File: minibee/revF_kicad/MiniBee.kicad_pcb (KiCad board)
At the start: 2 copper layers, 26.5 x 34 mm, 39 parts, among them IC1 MEGA8-AI, U1 ADXL345

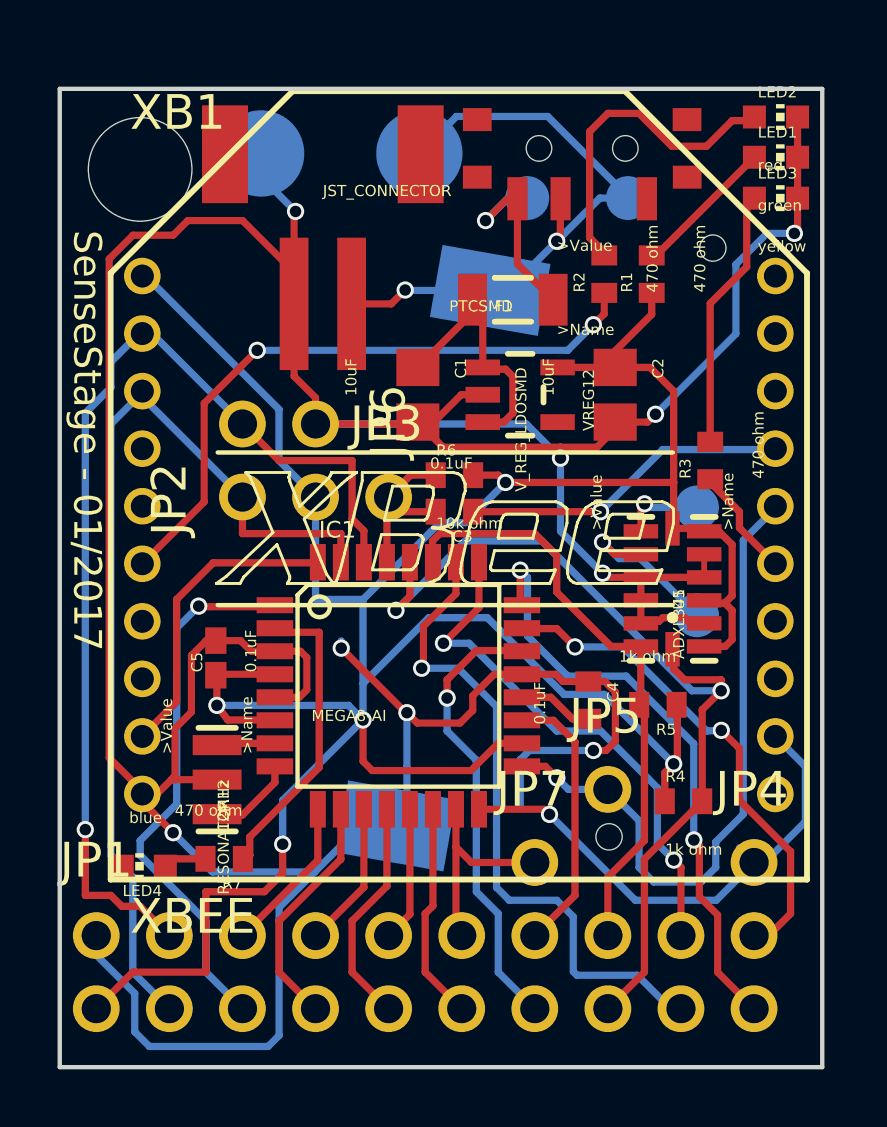
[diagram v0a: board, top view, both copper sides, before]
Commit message: updates to board: exchanged D2 and D7, other switch
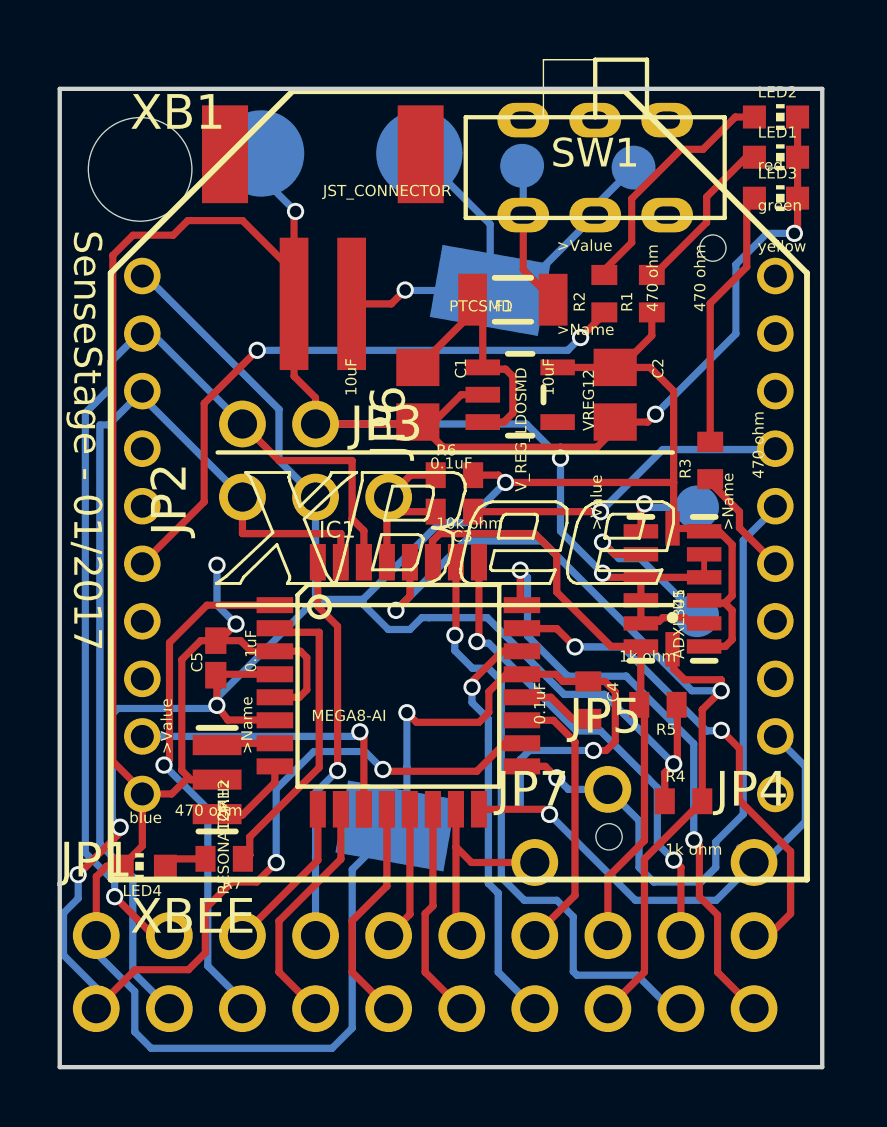
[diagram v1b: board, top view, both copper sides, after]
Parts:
- removed SWITCH12: MYSHIT_PCM_SWITCH, MYSHIT_PCM_SWITCH_RA
- added SW1: Switch_SPDT_x2, alps:alps_switch, F.Cu at (153.9, 90.7)
- moved JP11 1.14 mm to (151.3, 90.7)
- moved JP10 1.08 mm to (155.2, 90.7)
- moved R1 0.68 mm to (155.8, 95.1)
- moved R2 0.68 mm to (154.2, 95.1)
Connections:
- IC1 pad 32: /SLEEP -> /D2
- JP1 pad 8: /D7 -> /D2
- XB1 pad 9: /SLEEP -> /D7
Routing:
- net /D2: track 0.00 -> 13.6 mm, vias 0 -> 1
- net /SLEEP: track 10.7 -> 0.00 mm
- net VCC: track 105.7 -> 113.4 mm, vias 5 -> 7
- net /D7: track 5.09 -> 10.4 mm, vias 0 -> 1
- net /N$4: track 21.7 -> 18.3 mm, vias 2 -> 1
- net GND: track 153.4 -> 156.4 mm
- net /N$6: track 11.2 -> 8.48 mm
- net /N$8: track 7.22 -> 5.52 mm, vias 1 -> 0
- net /A3: track 22.9 -> 21.2 mm
- net /A2: track 18.3 -> 16.6 mm
- net /A7: track 15.7 -> 14.5 mm
- net /N$3: track 4.99 -> 5.79 mm
- net /D3: track 19.0 -> 18.2 mm
- net /TX: track 33.2 -> 33.9 mm
- net /PWM0: track 22.4 -> 21.7 mm

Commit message: updated gerbers for revision F
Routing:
- net GND: track 156.4 -> 157.0 mm, vias 9 -> 10
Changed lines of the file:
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@@
     (thickness 1.6)
     (drawings 138)
-    (tracks 528)
+    (tracks 532)
     (zones 0)
     (modules 39)
@@
   )
   (gr_line (start 149.953 98.6356) (end 150.10925 98.596537) (layer Eco1.User) (width 0.15))
+  (via (at 157.7213 97.5487) (size 0.6) (drill 0.4) (layers Top Bottom) (net 1))
+  (segment (start 157.6705 97.0153) (end 157.6705 97.4979) (width 0.25) (layer Top) (net 1))
+  (segment (start 157.6705 97.4979) (end 157.7213 97.5487) (width 0.25) (layer Top) (net 1))
   (segment (start 146.928355 113.620882) (end 146.928355 113.180345) (width 0.25) (layer Bottom) (net 1))
   (segment (start 151.3137 108.3496) (end 150.7685 108.3496) (width 0.25) (layer Top) (net 1))
@@
   (segment (start 158.75 94.107) (end 159.8295 93.0275) (width 0.25) (layer Bottom) (net 1))
   (segment (start 158.75 96.52) (end 158.75 94.107) (width 0.25) (layer Bottom) (net 1))
-  (segment (start 155.956 99.314) (end 158.75 96.52) (width 0.25) (layer Bottom) (net 1))
+  (segment (start 155.956 99.314) (end 157.7213 97.5487) (width 0.25) (layer Bottom) (net 1))
+  (segment (start 157.7213 97.5487) (end 158.75 96.52) (width 0.25) (layer Bottom) (net 1))
   (via (at 155.956 99.314) (size 0.6) (drill 0.4) (layers Top Bottom) (net 1))
   (segment (start 155.6844 99.5856) (end 155.956 99.314) (width 0.25) (layer Top) (net 1))
@@
   (segment (start 158.8731 103.2616) (end 158.8731 102.6996) (width 0.254) (layer Top) (net 33))
   (segment (start 160.1211 104.5096) (end 158.8731 103.2616) (width 0.254) (layer Top) (net 33))
-  (segment (start 157.8571 100.1596) (end 157.8571 95.4606) (width 0.254) (layer Top) (net 34))
-  (segment (start 157.8571 95.4606) (end 159.1271 94.1906) (width 0.254) (layer Top) (net 34))
-  (segment (start 159.1271 94.1906) (end 159.1271 92.0316) (width 0.254) (layer Top) (net 34))
+  (segment (start 157.8571 100.1596) (end 157.8571 99.8167) (width 0.254) (layer Top) (net 34))
+  (segment (start 157.8571 99.8167) (end 159.1271 98.5467) (width 0.254) (layer Top) (net 34))
+  (segment (start 159.1271 98.5467) (end 159.1271 92.0316) (width 0.254) (layer Top) (net 34))
   (segment (start 159.1271 92.0316) (end 159.3811 91.7776) (width 0.254) (layer Top) (net 34))
   (segment (start 159.3811 91.7776) (end 159.3811 91.9046) (width 0.254) (layer Top) (net 34))

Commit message: update silkscreen to rev F
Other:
- board text added: "rev F 01/2017"
- board text removed: "rev E 01/2017"
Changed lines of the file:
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@@
   )
   (target plus (at 135.1915 122.047) (size 5) (width 0.15) (layer Edge.Cuts))
-  (gr_text "rev E\n01/2017" (at 142.0495 108.9025 90) (layer B.SilkS)
+  (gr_text "rev F\n01/2017" (at 142.0495 108.9025 90) (layer B.SilkS)
     (effects (font (size 1 1) (thickness 0.15)) (justify mirror))
   )
